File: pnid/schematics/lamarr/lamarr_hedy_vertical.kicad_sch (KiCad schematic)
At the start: 81 parts

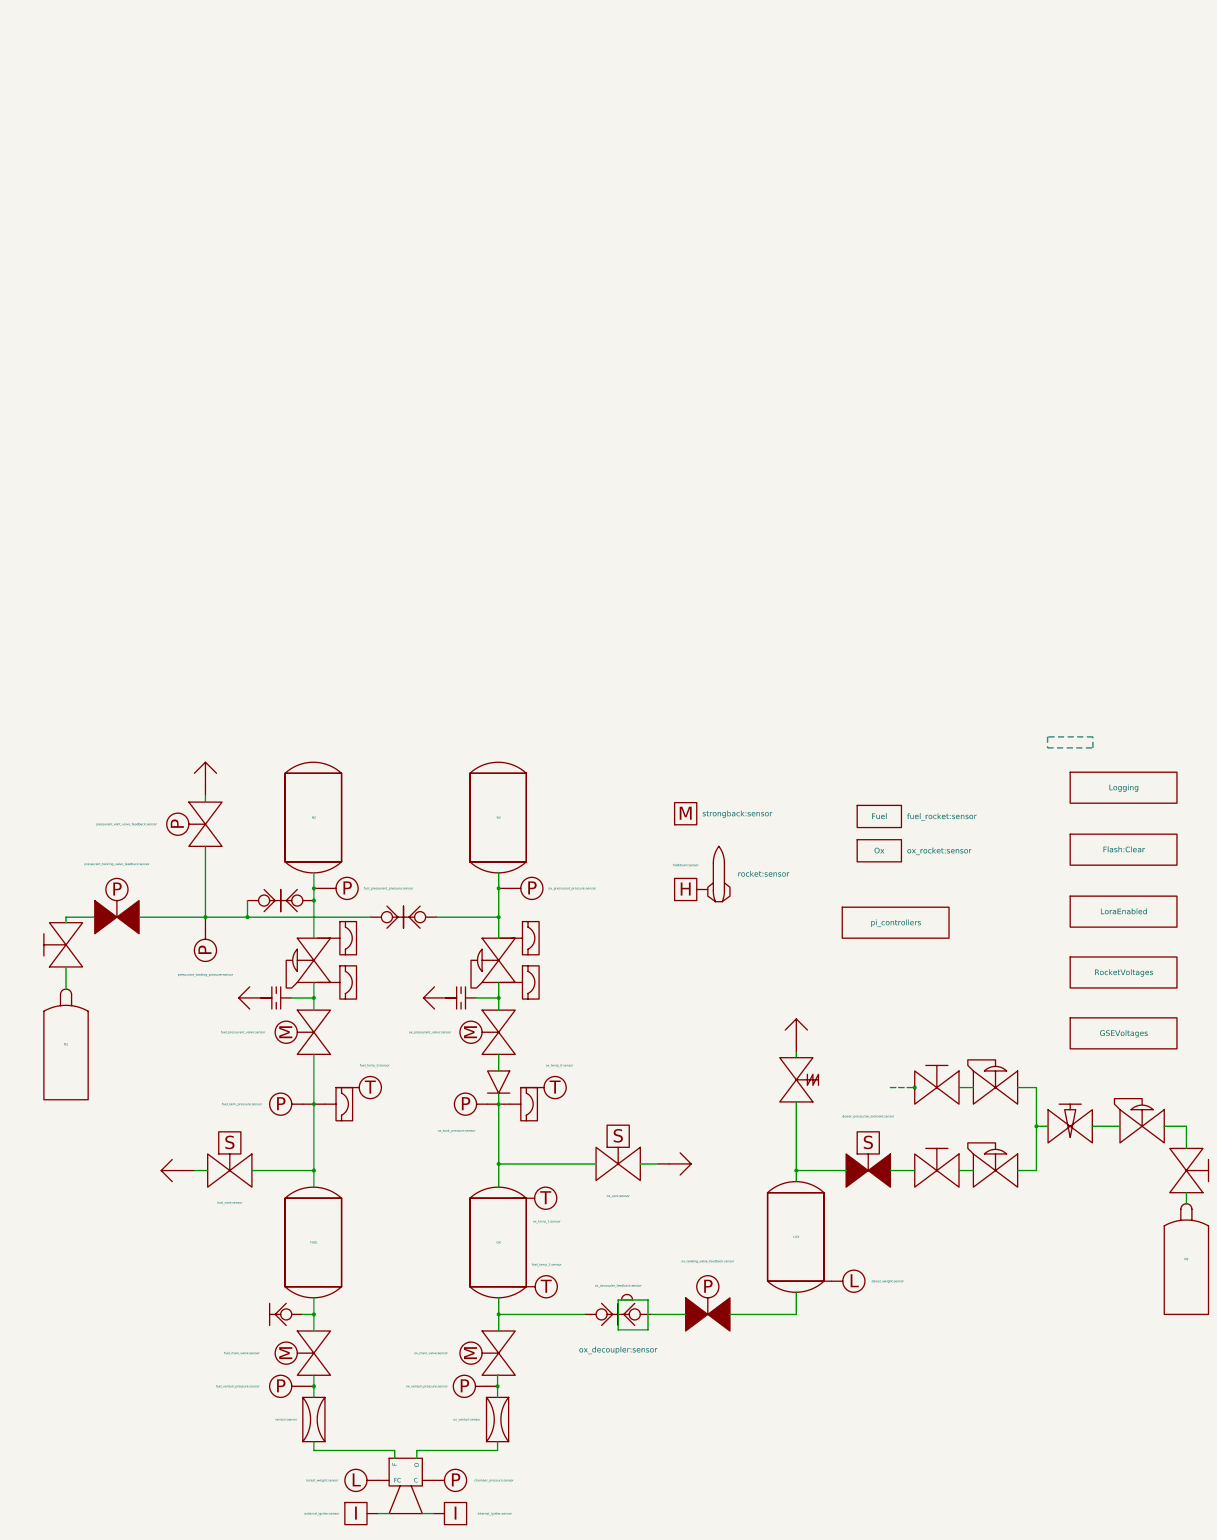
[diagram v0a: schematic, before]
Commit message: add vertical pnid with final flight configuration
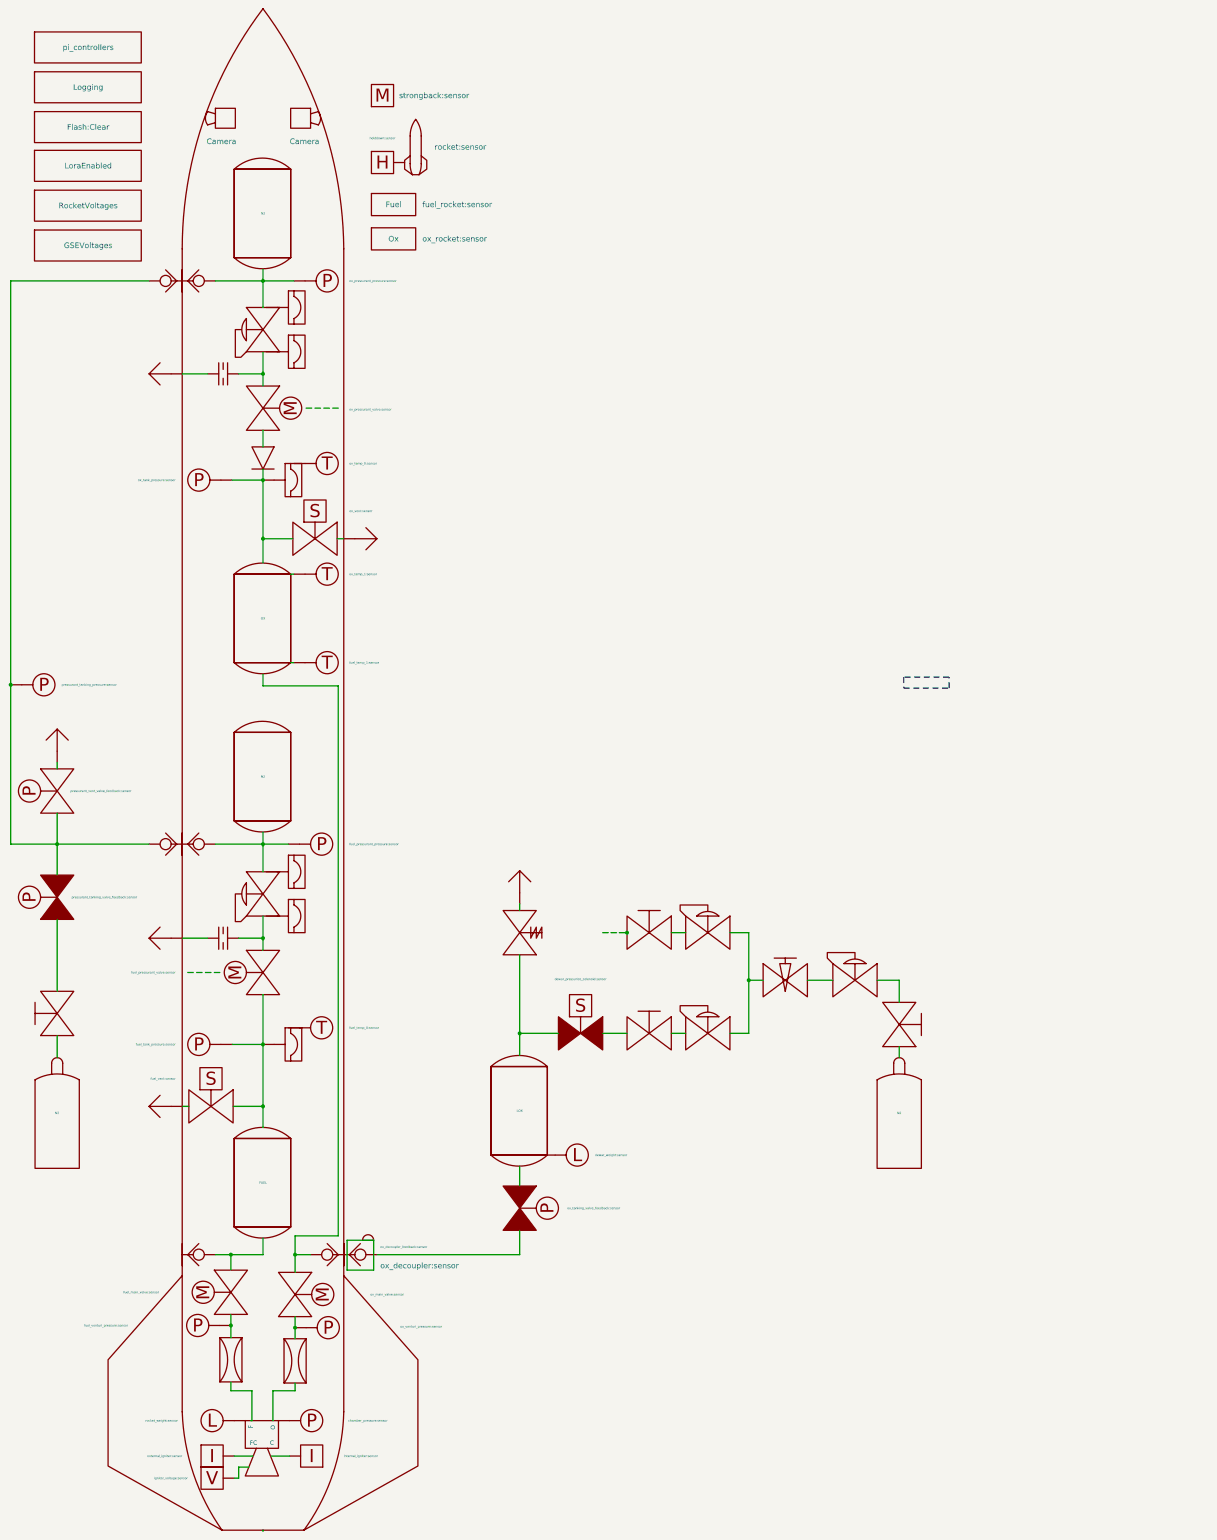
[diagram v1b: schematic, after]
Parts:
- added C6, C7: Camera, symbol PnID-Lib:Camera
- added U1: Rocket_Big, symbol PnID-Lib:Rocket_Big
- added voltmeter1: igniter_voltage:sensor, symbol PnID-Lib:voltmeter
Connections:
- net at engine.~ (O): now also venturi1.~; no longer chamber_pressure.~
- net at ox_venturi.~: now also ox_main_valve.~, ox_venturi_pressure.~; no longer engine.~ (O)
- net at thrust.~: no longer engine.~ (O)
- net at venturi1.~: now also fuel_main_valve.~, fuel_venturi_pressure.~; no longer engine.~ (O)
- net at dewar_needle_valve?.~: now also C2.~, C3.~; no longer C1.~
- net at Orifice2.~: now also Vent5.~
- net at Vent4.~: now also Orifice1.~
- new net: engine.~ (O), ox_venturi.~
- new net: OX.~, ox_main_valve.~, ox_quick_connect.~
- new net: DewarOverPressureValve?.~, LOX.~, dewar_pressurize_solenoid.~
- new net: C1.~, dewar_needle_valve?.~
- new net: DewarQuickConnect2.~, ox_quick_connect2.~, pressurant_tanking_pressure.~, pressurant_tanking_valve_(A1).~, pressurant_vent_valve_(A2).~
- new net: N2.~, ox_pressurant_pressure.~, ox_quick_connect3.~, pressurantPressureRegulator2.~
- new net: Orifice1.~, ox_pressurant_valve.~, pressurantPressureRegulator2.~
- new net: FUEL.~, fuel_main_valve.~, ox_quick_connect1.~
- new net: Orifice2.~, fuel_pressurant_valve.~, pressurantPressureRegulator1.~
- now unconnected: N2.~
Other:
- moved on the sheet: FUEL, Fuel, LOX, N2, OX, Ox

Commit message: fix in dewar (de)press solenoids, align pnid to 25mil grid
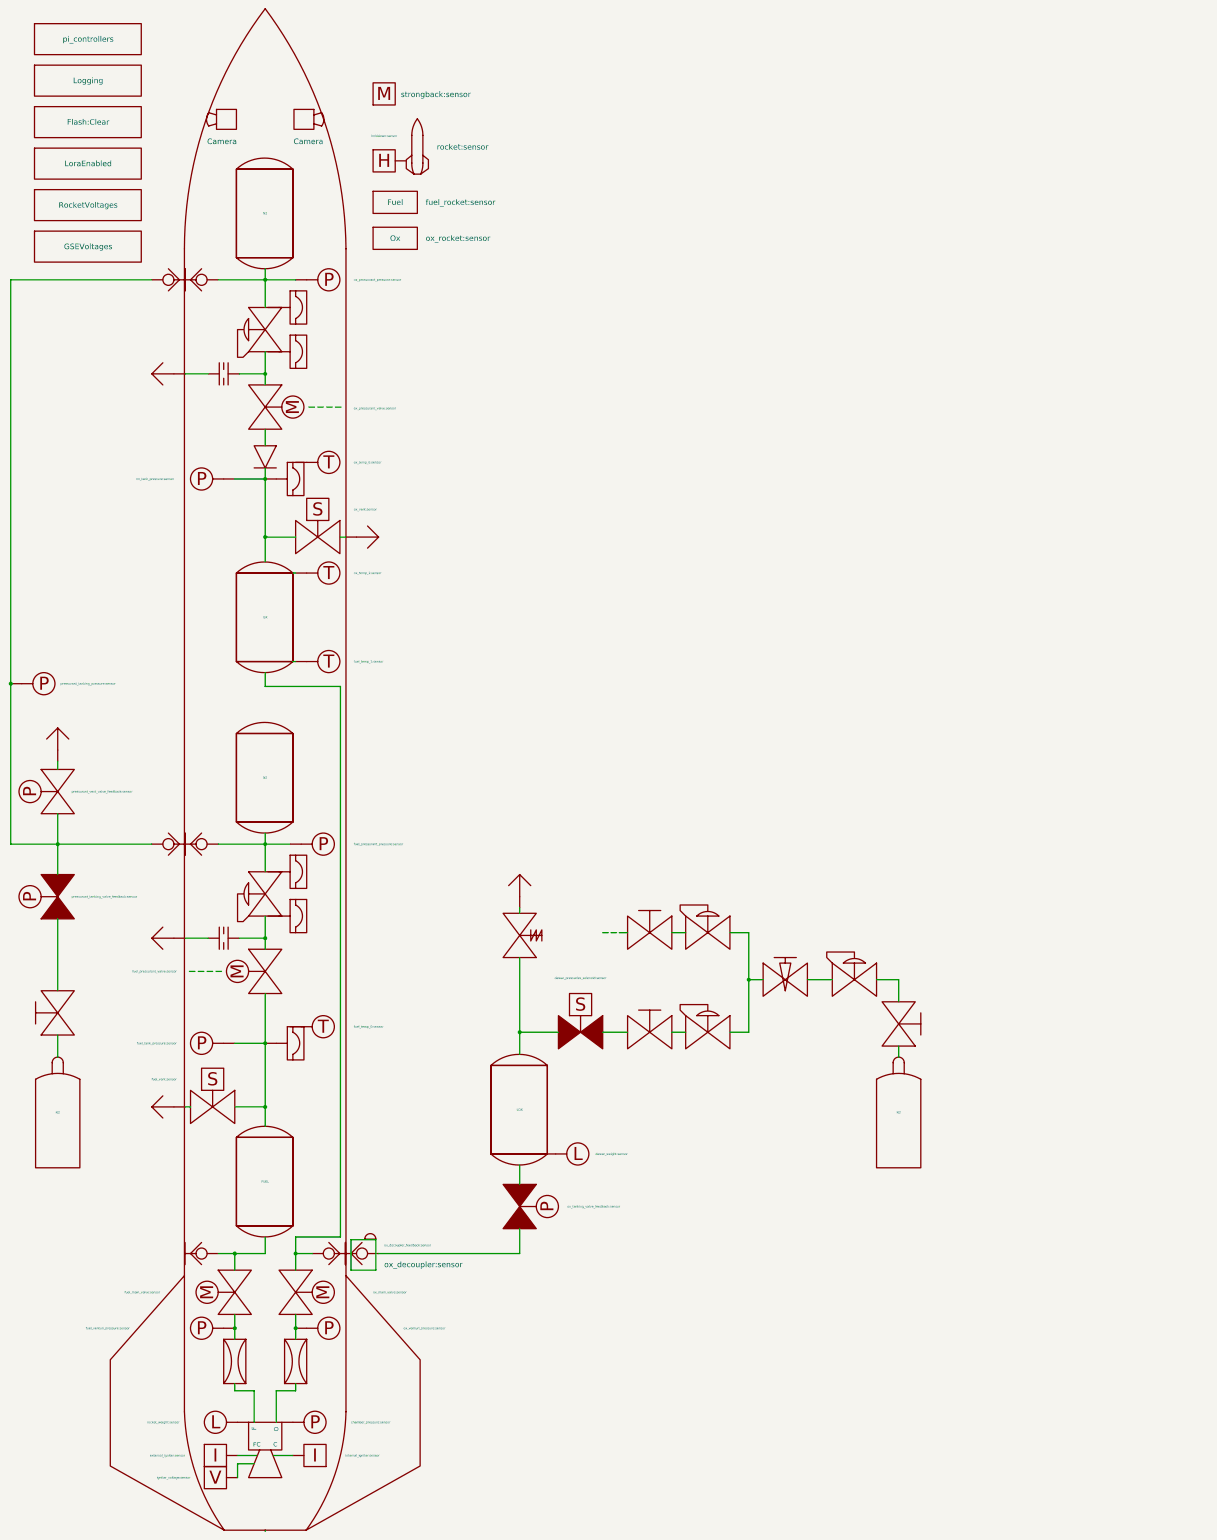
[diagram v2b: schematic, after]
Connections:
- net at engine.~ (O): now also venturi1.~
- net at ox_venturi.~: now also ox_main_valve.~, ox_venturi_pressure.~; no longer engine.~ (O)
- net at venturi1.~: now also fuel_main_valve.~, fuel_venturi_pressure.~; no longer engine.~ (O)
- net at dewar_needle_valve?.~: now also C2.~, C3.~; no longer C1.~
- new net: engine.~ (O), ox_venturi.~
- new net: OX.~, ox_main_valve.~, ox_quick_connect.~
- new net: DewarOverPressureValve?.~, LOX.~, dewar_pressurize_solenoid.~
- new net: C1.~, dewar_needle_valve?.~
- new net: Orifice1.~, ox_pressurant_valve.~, pressurantPressureRegulator2.~
- new net: FUEL.~, fuel_main_valve.~, ox_quick_connect1.~
- new net: Orifice2.~, fuel_pressurant_valve.~, pressurantPressureRegulator1.~
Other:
- moved on the sheet: FUEL, Fuel, N2, OX

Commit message: add rcu mapping, fix some state names in pnid, add GN pnids
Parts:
- C6: value Camera -> camera2:sensor
- C7: value Camera -> camera1:sensor
- voltmeter1: value igniter_voltage:sensor -> internal_igniter:sensor
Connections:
- net at engine.~ (O): now also venturi1.~
- net at ox_venturi.~: now also ox_main_valve.~, ox_venturi_pressure.~; no longer engine.~ (O)
- net at venturi1.~: now also fuel_main_valve.~, fuel_venturi_pressure.~; no longer engine.~ (O)
- net at dewar_needle_valve?.~: now also C2.~, C3.~; no longer C1.~
- new net: engine.~ (O), ox_venturi.~
- new net: OX.~, ox_main_valve.~, ox_quick_connect.~
- new net: DewarOverPressureValve?.~, LOX.~, dewar_pressurize_solenoid.~
- new net: C1.~, dewar_needle_valve?.~
- new net: Orifice1.~, ox_pressurant_valve.~, pressurantPressureRegulator2.~
- new net: FUEL.~, fuel_main_valve.~, ox_quick_connect1.~
- new net: Orifice2.~, fuel_pressurant_valve.~, pressurantPressureRegulator1.~
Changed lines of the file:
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@@
 	)
 	(symbol
-		(lib_name "PnID-Lib:Venturi")
 		(lib_id "PnID-Lib:Venturi")
 		(at 74.295 158.115 270)
@@
 	)
 	(symbol
-		(lib_name "PnID-Lib:Tank_Slim")
 		(lib_id "PnID-Lib:Tank_Slim")
 		(at 125.73 100.33 0)
@@
 	)
 	(symbol
-		(lib_name "PnID-Lib:PressureRegulator")
 		(lib_id "PnID-Lib:PressureRegulator")
 		(at 202.565 70.485 0)
@@
 	)
 	(symbol
-		(lib_name "PnID-Lib:Valve_Manual")
 		(lib_id "PnID-Lib:Valve_Manual")
 		(at 212.725 80.645 270)
@@
 	)
 	(symbol
-		(lib_name "PnID-Lib:PressureRegulator")
 		(lib_id "PnID-Lib:PressureRegulator")
 		(at 67.31 -78.74 90)
@@
 	)
 	(symbol
-		(lib_name "PnID-Lib:Tank_Slim")
 		(lib_id "PnID-Lib:Tank_Slim")
 		(at 67.31 -105.41 0)
@@
 			)
 		)
-		(property "Value" "Camera"
+		(property "Value" "camera1:sensor"
 			(at 53.975 -121.92 0)
 			(effects
@@
 	)
 	(symbol
-		(lib_name "PnID-Lib:Orifice")
 		(lib_id "PnID-Lib:Orifice")
 		(at 57.785 60.96 0)
@@
 	)
 	(symbol
-		(lib_name "PnID-Lib:Valve_Solenoid_NO")
 		(lib_id "PnID-Lib:Valve_Solenoid_NO")
 		(at 55.245 99.695 0)
@@
 	)
 	(symbol
-		(lib_name "PnID-Lib:Valve_Servo")
 		(lib_id "PnID-Lib:Valve_Servo")
 		(at 74.295 142.24 270)
@@
 	)
 	(symbol
-		(lib_name "PnID-Lib:Valve_Solenoid_NO")
 		(lib_id "PnID-Lib:Valve_Solenoid_NO")
 		(at 79.375 -31.115 0)
@@
 	)
 	(symbol
-		(lib_name "PnID-Lib:Tank_Slim")
 		(lib_id "PnID-Lib:Tank_Slim")
 		(at 67.31 24.13 0)
@@
 	)
 	(symbol
-		(lib_name "PnID-Lib:Valve_Servo")
 		(lib_id "PnID-Lib:Valve_Servo")
 		(at 67.31 68.58 90)
@@
 	)
 	(symbol
-		(lib_name "PnID-Lib:Tank_Slim")
 		(lib_id "PnID-Lib:Tank_Slim")
 		(at 67.31 116.84 0)
@@
 			)
 		)
-		(property "Value" "igniter_voltage:sensor"
+		(property "Value" "internal_igniter:sensor"
 			(at 50.165 184.785 0)
 			(effects
@@
 	)
 	(symbol
-		(lib_name "PnID-Lib:PressureRegulator")
 		(lib_id "PnID-Lib:PressureRegulator")
 		(at 168.91 59.69 0)
@@
 	)
 	(symbol
-		(lib_name "PnID-Lib:Venturi")
 		(lib_id "PnID-Lib:Venturi")
 		(at 60.325 158.115 270)
@@
 	)
 	(symbol
-		(lib_name "PnID-Lib:Valve_Servo")
 		(lib_id "PnID-Lib:Valve_Servo")
 		(at 67.31 -60.96 270)
@@
 			)
 		)
-		(property "Value" "Camera"
+		(property "Value" "camera2:sensor"
 			(at 80.645 -121.92 0)
 			(effects
@@
 	)
 	(symbol
-		(lib_name "PnID-Lib:Valve_Servo")
 		(lib_id "PnID-Lib:Valve_Servo")
 		(at 60.325 142.24 90)
@@
 	)
 	(symbol
-		(lib_name "PnID-Lib:Valve_Manual")
 		(lib_id "PnID-Lib:Valve_Manual")
 		(at 155.575 82.55 0)
@@
 	)
 	(symbol
-		(lib_name "PnID-Lib:PressureRegulator")
 		(lib_id "PnID-Lib:PressureRegulator")
 		(at 67.31 50.8 90)
@@
 	)
 	(symbol
-		(lib_name "PnID-Lib:PressureRegulator")
 		(lib_id "PnID-Lib:PressureRegulator")
 		(at 168.91 82.55 0)
@@
 	)
 	(symbol
-		(lib_name "PnID-Lib:Orifice")
 		(lib_id "PnID-Lib:Orifice")
 		(at 57.785 -68.58 0)
@@
 	)
 	(symbol
-		(lib_name "PnID-Lib:Valve_Manual")
 		(lib_id "PnID-Lib:Valve_Manual")
 		(at 19.685 78.105 90)
@@
 	)
 	(symbol
-		(lib_name "PnID-Lib:Tank_Slim")
 		(lib_id "PnID-Lib:Tank_Slim")
 		(at 67.31 -12.7 0)
@@
 	)
 	(symbol
-		(lib_name "PnID-Lib:Valve_Manual")
 		(lib_id "PnID-Lib:Valve_Manual")
 		(at 155.575 59.69 0)

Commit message: update pnids, add main lora pnid, fix camera config
fix some minor issues in pnid state names (igniters)
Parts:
- added voltmeter2: internal_igniter_2:sensor, symbol PnID-Lib:voltmeter
- C6: value camera2:sensor -> camera_2:sensor
- C7: value camera1:sensor -> camera_1:sensor
- igniter1: value external_igniter:sensor -> internal_igniter_1_cont:sensor
- igniter2: value internal_igniter:sensor -> internal_igniter_2_cont:sensor
- voltmeter1: value internal_igniter:sensor -> internal_igniter_1:sensor
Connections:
- net at engine.~ (O): now also venturi1.~
- net at ox_venturi.~: now also ox_main_valve.~, ox_venturi_pressure.~; no longer engine.~ (O)
- net at venturi1.~: now also fuel_main_valve.~, fuel_venturi_pressure.~; no longer engine.~ (O)
- net at dewar_needle_valve?.~: now also C2.~, C3.~; no longer C1.~
- new net: engine.~ (O), ox_venturi.~
- new net: OX.~, ox_main_valve.~, ox_quick_connect.~
- new net: DewarOverPressureValve?.~, LOX.~, dewar_pressurize_solenoid.~
- new net: C1.~, dewar_needle_valve?.~
- new net: Orifice1.~, ox_pressurant_valve.~, pressurantPressureRegulator2.~
- new net: FUEL.~, fuel_main_valve.~, ox_quick_connect1.~
- new net: Orifice2.~, fuel_pressurant_valve.~, pressurantPressureRegulator1.~

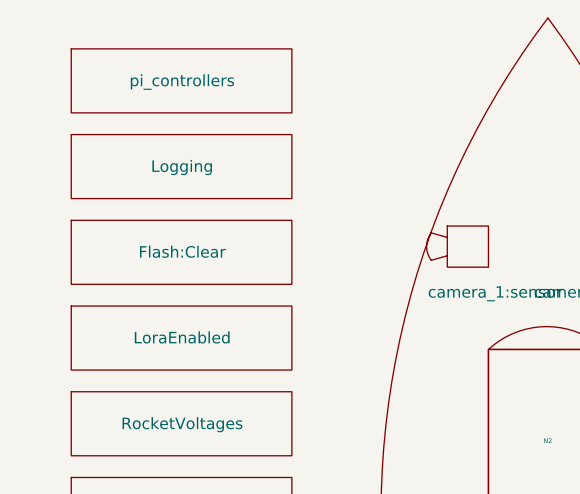
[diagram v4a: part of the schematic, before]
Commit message: various fixes
configure lora use,
fix guidance & navigation pnid,
fix retract threshold
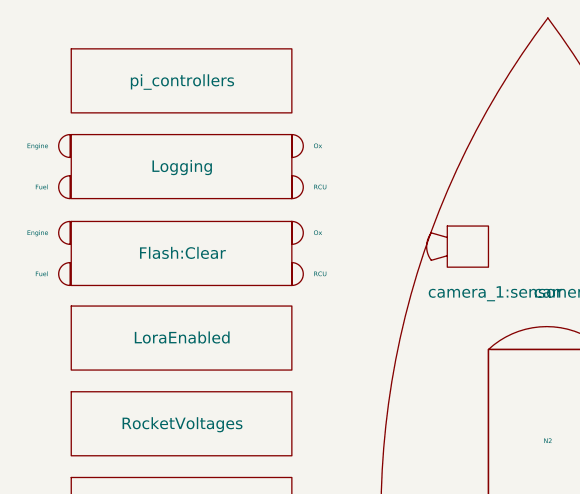
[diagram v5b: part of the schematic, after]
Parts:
- removed ClearFlash: Flash:Clear, symbol PnID-Lib:Label
- removed Logging: Logging, symbol PnID-Lib:Label
- added ClearFlash1: Flash:Clear, symbol PnID-Lib:Label
- added Engine: engine_ecu:LoggingEnabled, symbol PnID-Lib:LED
- added Engine: ecu:FlashStatus, symbol PnID-Lib:LED
- added Fuel: fuel_ecu:LoggingEnabled, symbol PnID-Lib:LED
- added Fuel: fuel_ecu:FlashStatus, symbol PnID-Lib:LED
- added Logging1: Logging, symbol PnID-Lib:Label
- added Ox: ox_ecu:LoggingEnabled, symbol PnID-Lib:LED
- added Ox: ox_ecu:FlashStatus, symbol PnID-Lib:LED
- added RCU: rcu:LoggingEnabled, symbol PnID-Lib:LED
- added RCU: rcu:FlashStatus, symbol PnID-Lib:LED
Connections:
- net at engine.~ (O): now also venturi1.~
- net at ox_venturi.~: now also ox_main_valve.~, ox_venturi_pressure.~; no longer engine.~ (O)
- net at venturi1.~: now also fuel_main_valve.~, fuel_venturi_pressure.~; no longer engine.~ (O)
- net at dewar_needle_valve?.~: now also C2.~, C3.~; no longer C1.~
- new net: engine.~ (O), ox_venturi.~
- new net: OX.~, ox_main_valve.~, ox_quick_connect.~
- new net: DewarOverPressureValve?.~, LOX.~, dewar_pressurize_solenoid.~
- new net: C1.~, dewar_needle_valve?.~
- new net: Orifice1.~, ox_pressurant_valve.~, pressurantPressureRegulator2.~
- new net: FUEL.~, fuel_main_valve.~, ox_quick_connect1.~
- new net: Orifice2.~, fuel_pressurant_valve.~, pressurantPressureRegulator1.~

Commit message: i mog schlafn
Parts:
- Engine: value ecu:FlashStatus -> engine_ecu:FlashStatus
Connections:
- net at engine.~ (O): now also venturi1.~
- net at ox_venturi.~: now also ox_main_valve.~, ox_venturi_pressure.~; no longer engine.~ (O)
- net at venturi1.~: now also fuel_main_valve.~, fuel_venturi_pressure.~; no longer engine.~ (O)
- net at dewar_needle_valve?.~: now also C2.~, C3.~; no longer C1.~
- new net: engine.~ (O), ox_venturi.~
- new net: OX.~, ox_main_valve.~, ox_quick_connect.~
- new net: DewarOverPressureValve?.~, LOX.~, dewar_pressurize_solenoid.~
- new net: C1.~, dewar_needle_valve?.~
- new net: Orifice1.~, ox_pressurant_valve.~, pressurantPressureRegulator2.~
- new net: FUEL.~, fuel_main_valve.~, ox_quick_connect1.~
- new net: Orifice2.~, fuel_pressurant_valve.~, pressurantPressureRegulator1.~
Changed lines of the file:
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@@
 			)
 		)
-		(property "Value" "ecu:FlashStatus"
+		(property "Value" "engine_ecu:FlashStatus"
 			(at 13.716 -131.064 90)
 			(effects
